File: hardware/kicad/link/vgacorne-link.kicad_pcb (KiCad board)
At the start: 2 copper layers, 33 x 13 mm, 5 parts, among them J1 DE-15F (VGA), J2 JST-SH pigtail

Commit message: Add trackpad, mouse column and scroll wheel; move MCU and ports
Layout
- MCU module, USB-C and trackpad move to the right half; the left half
  is now the passive satellite.
- VGA daughterboard bay moves to the inner-back corner so both cables
  leave from the back face. The bay sits 4.5 mm further back than the
  keys need, so both halves are 116 mm deep.
- Azoteq TPS65 trackpad, landscape, right beside Y/H/N under a 1 mm
  overlay. The MCU module moves to a PCB ear behind it, next to the
  VGA bay. trackpad.py selects the pad (TPS65 or 40 mm Cirque); the
  case pocket, J5 connector and QMK driver follow the selection.
- Left half: a mouse column beside T/G/B with a scroll wheel (Bourns
  PEC12R) at the top and left/right-click HE keys beside G and B.

Circuits and firmware
- Mux channels reassigned so the satellite's mouse keys and wheel fill
  its three spare channels. The wheel's A/B contacts are summed into
  four voltage levels on one channel.
- QMK: 44-key LAYOUT and a wheel decoder that feeds QMK's quadrature
  encoder driver. Trackpad on I2C1, with rules.mk now generated. The
  host test covers the wheel.
- libhmk: MS_BTN1/MS_BTN2 on the mouse keys (no encoder support).

Case and renders
- Smoother milled case: 7.25 mm walls, 25 mm minimum outside radius
  and a flat back face at the ports.
- render.py builds Blender Cycles renders from the design geometry.

Co-Authored-By: Claude Opus 5.5 (1M context) <noreply@anthropic.com>
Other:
- board text added: "VGACorne"
- board text removed: "VGACorne link"

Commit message: Use the Amphenol FCI 10090929-S154XLF VGA socket
A vertical HD-15 socket with 4-40 clinch nuts and board locks, in stock
at Digi-Key. The board locks, soldered into the plated mounting holes,
tie the shell (and through the jackscrews, the case) to GND. The library
gains a copy of KiCad's vertical HD-15 footprint with the 1.2 mm pin
holes and 3.1 mm board-lock holes Amphenol specifies.

Keystone 7229 jackscrews (0.187" hex, 0.25" stud) fix it to the 1.6 mm
wall; the docs cover soldering the board locks, clipping the pin tails
and checking the board-to-flange height on the first part.

Co-Authored-By: Claude Opus 5.5 (1M context) <noreply@anthropic.com>
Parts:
- J1: value DE-15F (VGA) -> 10090929-S154XLF; footprint Connector_Dsub:DSUB-15-HD_Socket_Vertical_P2.29x1.98mm_MountingHoles -> vgacorne:DSUB-15-HD_Socket_Vertical_P2.29x1.98mm_Amphenol_10090929

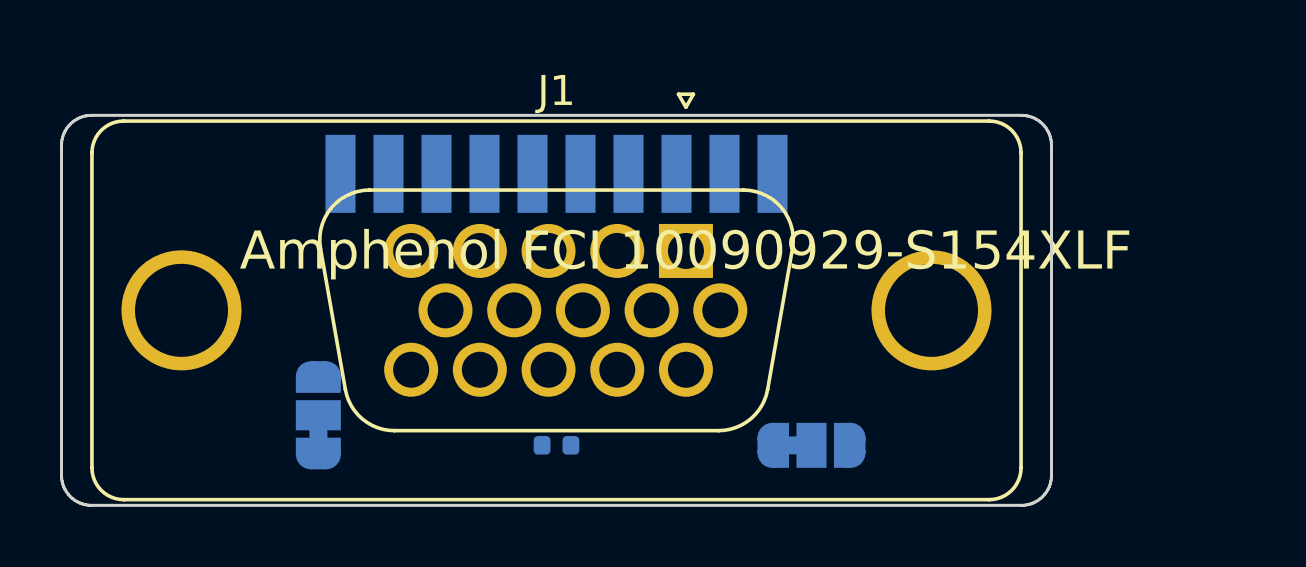
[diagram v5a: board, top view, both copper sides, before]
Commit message: Route the VGA daughterboard with Freerouting
hardware/route.py drives Freerouting directly (the KiCad MCP's autorouter
trips over a pcbnew/Python 3.14 binding bug): signals first with the
ground pours as planes, then ground as tracks round the locked signals,
then the pours and ground stitching vias. The daughterboard routes
completely and passes DRC.

To make it routable:
- the 10-pin link order now follows the DE-15 under the pigtail pads
  (J3 on both halves follows; the pigtail stays 1:1, +5 V on pin 1);
- the pigtail pads are shorter and at the board edge, leaving a via
  channel above the connector;
- the socket keeps KiCad's 1.6 mm pads round Amphenol's 1.2 mm holes,
  so a track fits between pins;
- both cable-variant jumpers sit together by pins 9 and 15.

generate.py --force pcbs now leaves boards with tracks alone.

Co-Authored-By: Claude Opus 5.5 (1M context) <noreply@anthropic.com>
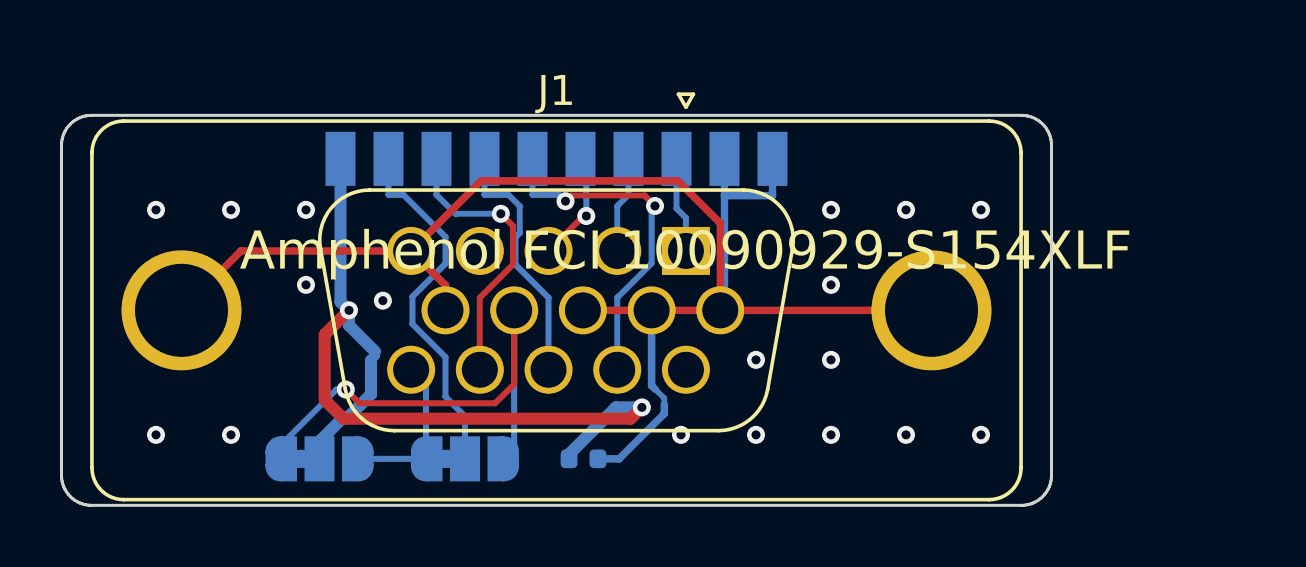
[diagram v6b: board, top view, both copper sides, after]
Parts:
- moved JP2 11.6 mm to (92.6, 106.9)
- moved JP1 1.45 mm to (87.8, 106.9), turned to 0 degrees
- moved C1 1.01 mm to (96.6, 106.9)
- moved J2 0.50 mm to (95.7, 96.9)
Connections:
- J2 pad 10: /LINK_C -> GND
- J2 pad 2: GND -> /LINK_DET
- J2 pad 3: /LINK_S0 -> /LINK_S1
- J2 pad 4: /LINK_S1 -> /LINK_S0
- J2 pad 6: /LINK_DET -> /LINK_C
- J2 pad 7: GND -> /LINK_B
- J2 pad 9: /LINK_B -> GND
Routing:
- net GND: track 0.00 -> 51.7 mm, vias 0 -> 18
- net /+5V_LINK: track 0.00 -> 28.9 mm, vias 0 -> 2
- net /VGA_P9: track 0.00 -> 17.0 mm, vias 0 -> 1
- net /LINK_DET: track 0.00 -> 12.3 mm
- net /LINK_S2: track 0.00 -> 11.6 mm, vias 0 -> 2
- net /LINK_S1: track 0.00 -> 9.43 mm, vias 0 -> 1
- net /LINK_S0: track 0.00 -> 8.50 mm
- net /VGA_P15: track 0.00 -> 5.43 mm
- net /LINK_C: track 0.00 -> 3.73 mm, vias 0 -> 1
- net /LINK_B: track 0.00 -> 3.23 mm
- net /LINK_A: track 0.00 -> 3.20 mm

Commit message: Make the MCU modules 4-layer and route them
The modules are now 1.0 mm 4-layer boards with a solid GND plane on In1
and +3V3 on In2, so every cap and supply pin drops a via and the signals,
USB included, run over unbroken ground. Their support parts are placed
beside the LQFP pins they serve (each 100 nF at its supply pin, the
crystal at the oscillator pins). Module net classes: 0.15 mm clearance,
USB 0.2/0.15 mm (~91 ohm over the plane on JLC's 1.0 mm stack-up).
Castellated pads connect solidly to the planes.

route.py learns to route to castellated edge pads (routing area grown
past the edge, keepouts holding the copper-to-edge clearance), to fan
plane-net pads out to their own vias before routing, and to fall back to
one-pass routing on 2-layer boards. Both modules route completely and
pass DRC.

Also: part-number and tolerance fields no longer print on the
silkscreen.

Co-Authored-By: Claude Opus 5.5 (1M context) <noreply@anthropic.com>
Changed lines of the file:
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@@
 			(at 0 0 0)
 			(layer "F.SilkS")
+			(hide yes)
 			(effects
 				(font
